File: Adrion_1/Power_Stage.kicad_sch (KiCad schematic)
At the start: 96 parts, among them IC2 UCC21521DW, IC3 UCC21521DW, J1 1705469, J2 1705469, Q1 IPP111N15N3GXKSA1, Q2 IPP111N15N3GXKSA1, Q3 IPP111N15N3GXKSA1, Q5 IPP111N15N3GXKSA1, U5 CKSR_6-NP

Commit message: Routing, Placement, Datasheets actualizado
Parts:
- removed C39: 4.7 uF, MKP1F044706J00JSSD:MKP1F044706J00JSSD, symbol MKP1F044706J00JSSD:MKP1F044706J00JSSD
- removed C41: MKP1F044706J00JSSD, MKP1F044706J00JSSD, symbol MKP1F044706J00JSSD:MKP1F044706J00JSSD
- added C36, C37, C39, C59: C5750X6S2W225K250KA, C5750_Commercial:C5750_Commercial, symbol C5750X6S2W225K250KA:C5750X6S2W225K250KA
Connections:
- net GNDPWR: now also C36.1, C37.1, C39.1, C59.1
- net HV: now also C36.2, C37.2, C39.2, C59.2

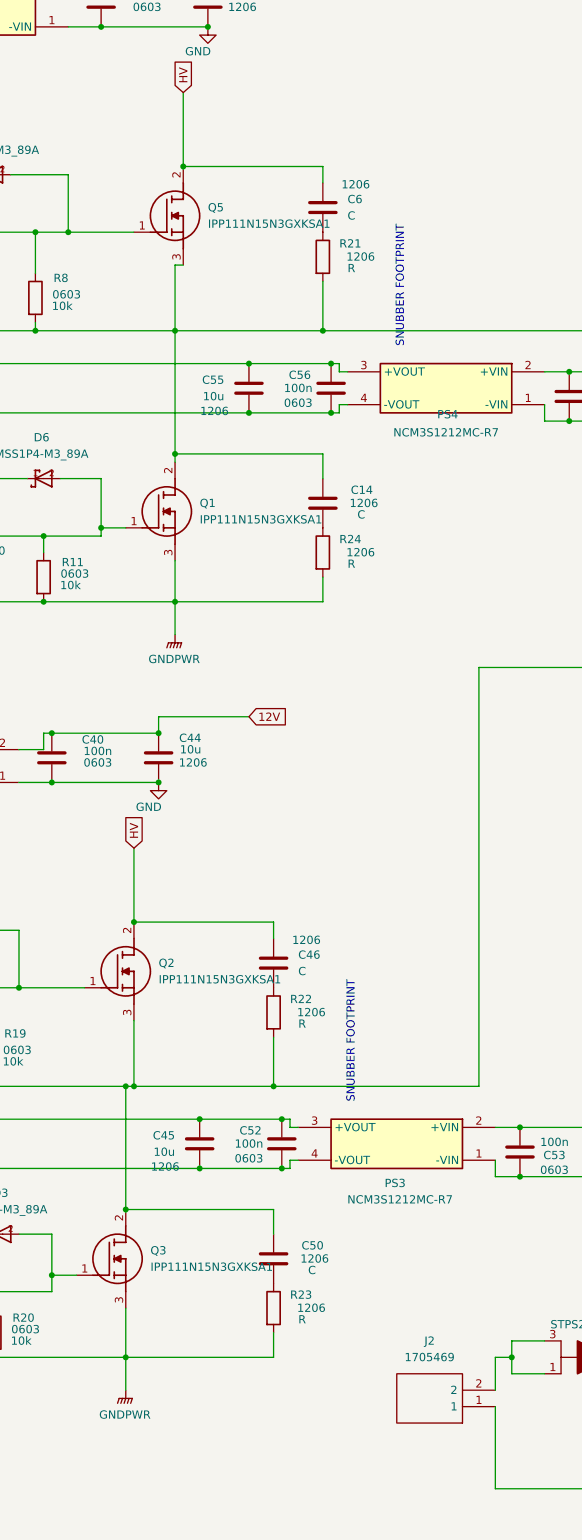
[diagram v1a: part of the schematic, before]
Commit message: arrreglos, venitilador y disipadores primera version
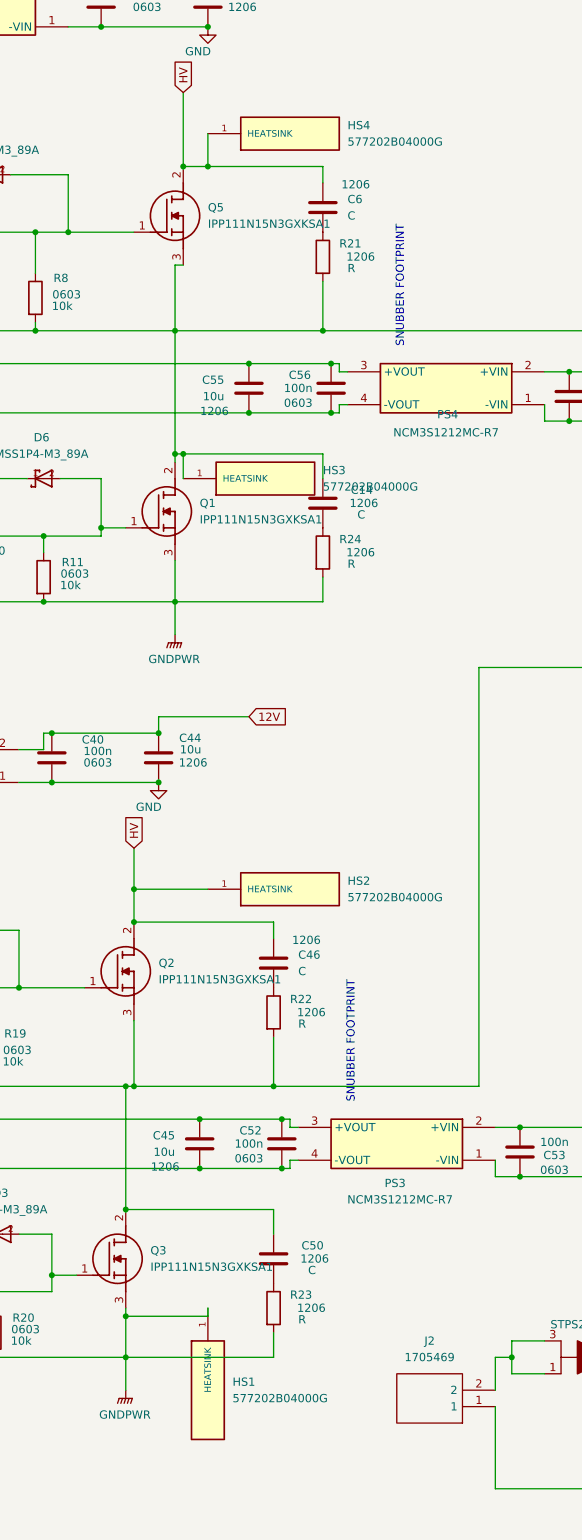
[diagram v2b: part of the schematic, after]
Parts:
- added HS1, HS2, HS3, HS4: 577202B04000G, HSINK_577202B04000G:HSINK_577202B04000G, symbol 577202B04000G:577202B04000G
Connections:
- net GNDPWR: now also HS1.1 (HEATSINK)
- net HV: now also HS2.1 (HEATSINK), HS4.1 (HEATSINK)
- net at C12.1, C14.1, C19.2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: now also HS3.1 (HEATSINK)

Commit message: FirstPrototype
First Prototype sent
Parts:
- removed C27, C28, C29, C30, C31, C32, C33: B43547F2108M067, CAPPRD1000W190D3550H4200:CAPPRD1000W190D3550H4200, symbol B43547F2108M067:B43547F2108M067
- removed C38: 1000u, CAPPRD1000W190D3550H4200:CAPPRD1000W190D3550H4200, symbol B43547F2108M067:B43547F2108M067
- removed HS1, HS2, HS3, HS4: 577202B04000G, HSINK_577202B04000G:HSINK_577202B04000G, symbol 577202B04000G:577202B04000G
- removed J1, J2: 1705469, 1705469:1705469, symbol 1705469:1705469
- removed R26, R27, R28: CRCW251215K0FKEG, RESC6332X70N:RESC6332X70N, symbol CRCW251215K0FKEG:CRCW251215K0FKEG
- added C27, C28, C29, C30, C31, C32, C41, C60: LGU2D102MELA, LGU2D102MELA:LGU2D102MELA, symbol LGU2D102MELA:LGU2D102MELA
- added J1, J2, J4, J5: 7462810, 7462810:7462810, symbol 7462810:7462810
- added R26, R27, R29: CRGP2512F15K, RESC6332X65N:RESC6332X65N, symbol CRGP2512F15K:CRGP2512F15K
- D8: value STPS20200CTN -> SDT40A120CT; footprint TO255P460X1020X1905-3P:TO255P460X1020X1905-3P -> TO254P1066X482X2286-3:TO254P1066X482X2286-3
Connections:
- net GNDPWR: now also C27.2 (-), C28.2 (-), C29.2 (-), C30.2 (-), C31.2 (-), C32.2 (-), C41.2 (-), C60.2 (-), J2.1, J2.2, J2.3, J2.4, R26.2, R27.2, R29.2
- net HV: now also C27.1 (+), C28.1 (+), C29.1 (+), C30.1 (+), C31.1 (+), C32.1 (+), C41.1 (+), C60.1 (+), R26.1, R27.1, R29.1
- net at C15.2, C16.2, C20.2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: now also J5.1, J5.2, J5.3, J5.4
- net at D8.1, D8.3: now also J4.1, J4.2, J4.3, J4.4
- net at U5.6 (OUT_1), U5.7 (OUT_2), U5.8 (OUT_3)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: now also J1.1, J1.2, J1.3, J1.4
- no-connect marks 6 -> 8
